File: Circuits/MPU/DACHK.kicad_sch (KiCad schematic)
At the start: 29 parts, among them J12 Conn_02x03_Odd_Even, U1 ProASIC, U11 AD5328, U12 MAX308CSE+, U13 MAX308CSE+, U14 ADA4805-2ARMZ, U15 AD7984BRMZ

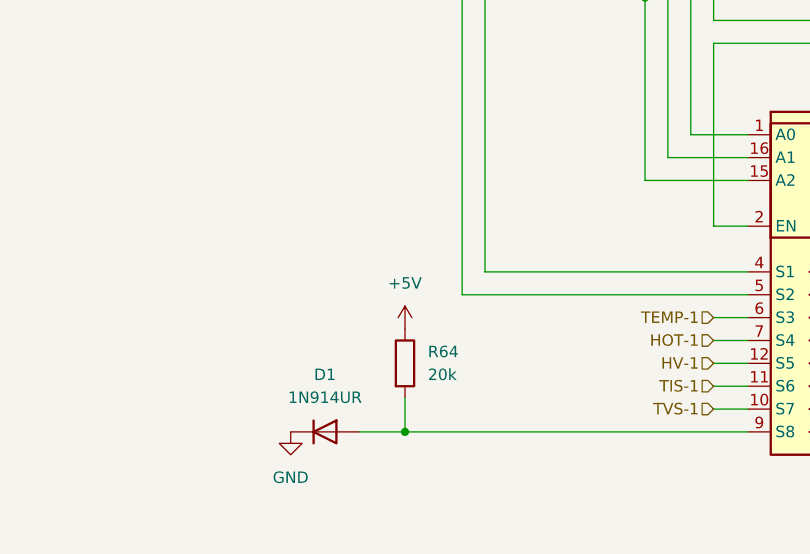
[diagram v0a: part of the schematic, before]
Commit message: fix MPU temp sensor bias
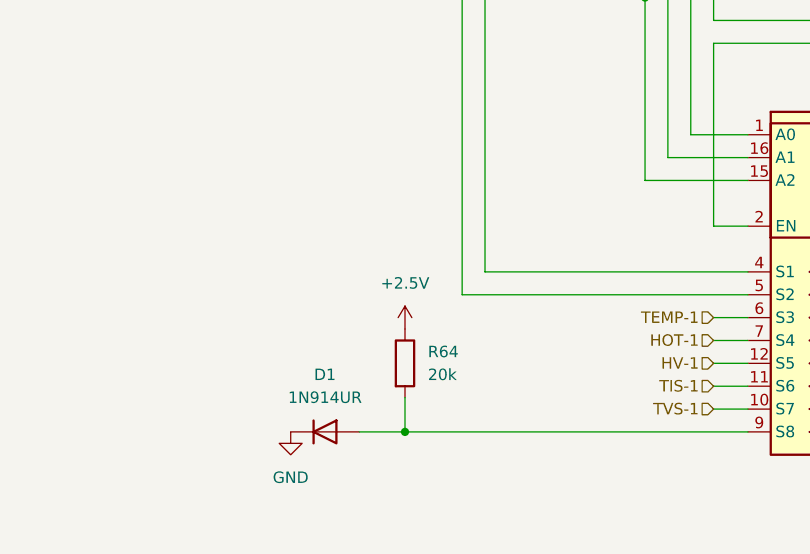
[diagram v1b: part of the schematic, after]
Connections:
- net +5V: no longer R64.1
- new net +2.5V: R64.1
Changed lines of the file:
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@@
 		(title "QuERI MPU")
 		(date "2024-07-10")
-		(rev "RR4")
+		(rev "Draft")
 		(company "Noqsi Aerospace Ltd")
 		(comment 1 "15 Blanchard Avenue, Billerica MA 01821")
@@
 	)
 	(symbol
+		(lib_id "QuERI_symbols:+2.5F")
+		(at 69.85 179.07 0)
+		(unit 1)
+		(exclude_from_sim no)
+		(in_bom yes)
+		(on_board yes)
+		(dnp no)
+		(fields_autoplaced yes)
+		(property "Reference" "#PWR094"
+			(at 69.85 182.88 0)
+			(effects
+				(font
+					(size 1.27 1.27)
+				)
+				(hide yes)
+			)
+		)
+		(property "Value" "+2.5V"
+			(at 69.85 173.99 0)
+			(effects
+				(font
+					(size 1.27 1.27)
+				)
+			)
+		)
+		(property "Footprint" ""
+			(at 69.85 179.07 0)
+			(effects
+				(font
+					(size 1.27 1.27)
+				)
+				(hide yes)
+			)
+		)
+		(property "Datasheet" ""
+			(at 69.85 179.07 0)
+			(effects
+				(font
+					(size 1.27 1.27)
+				)
+				(hide yes)
+			)
+		)
+		(property "Description" "Power symbol creates a global label with name \"+2.5F\""
+			(at 69.85 179.07 0)
+			(effects
+				(font
+					(size 1.27 1.27)
+				)
+				(hide yes)
+			)
+		)
+		(pin "1"
+		)
+		(instances
+			(project "MPU"
+				(path "/a3d8c1ad-4320-4fce-bd93-27782a1083f9/9e58b4b2-62c5-43c0-a04c-5a5353afcf88"
+					(reference "#PWR094")
+					(unit 1)
+				)
+			)
+		)
+	)
+	(symbol
 		(lib_id "QuERI_symbols:AD5328")
 		(at 62.23 82.55 0)
@@
 					(unit 1)
 				)
-			)
-		)
-	)
-	(symbol
-		(lib_id "power:+5V")
-		(at 69.85 179.07 0)
-		(unit 1)
-		(exclude_from_sim no)
-		(in_bom yes)
-		(on_board yes)
-		(dnp no)
-		(fields_autoplaced yes)
-		(property "Reference" "#PWR094"
-			(at 69.85 182.88 0)
-			(effects
-				(font
-					(size 1.27 1.27)
-				)
-				(hide yes)
-			)
-		)
-		(property "Value" "+5V"
-			(at 69.85 173.99 0)
-			(effects
-				(font
-					(size 1.27 1.27)
-				)
-			)
-		)
-		(property "Footprint" ""
-			(at 69.85 179.07 0)
-			(effects
-				(font
-					(size 1.27 1.27)
-				)
-				(hide yes)
-			)
-		)
-		(property "Datasheet" ""
-			(at 69.85 179.07 0)
-			(effects
-				(font
-					(size 1.27 1.27)
-				)
-				(hide yes)
-			)
-		)
-		(property "Description" "Power symbol creates a global label with name \"+5V\""
-			(at 69.85 179.07 0)
-			(effects
-				(font
-					(size 1.27 1.27)
-				)
-				(hide yes)
-			)
-		)
-		(pin "1"
-		)
-		(instances
-			(project "MPU"
-				(path "/a3d8c1ad-4320-4fce-bd93-27782a1083f9/9e58b4b2-62c5-43c0-a04c-5a5353afcf88"
-					(reference "#PWR094")
-					(unit 1)
-				)
